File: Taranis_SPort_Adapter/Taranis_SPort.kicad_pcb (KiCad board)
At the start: 2 copper layers, 22.9 x 17.8 mm, 12 parts, among them J1 CONN_01X04, J2 CONN_01X05, J3 CONN_01X04, Q1 DMG6602SVT, U1 MCP1754ST-3302E/MB-fixed

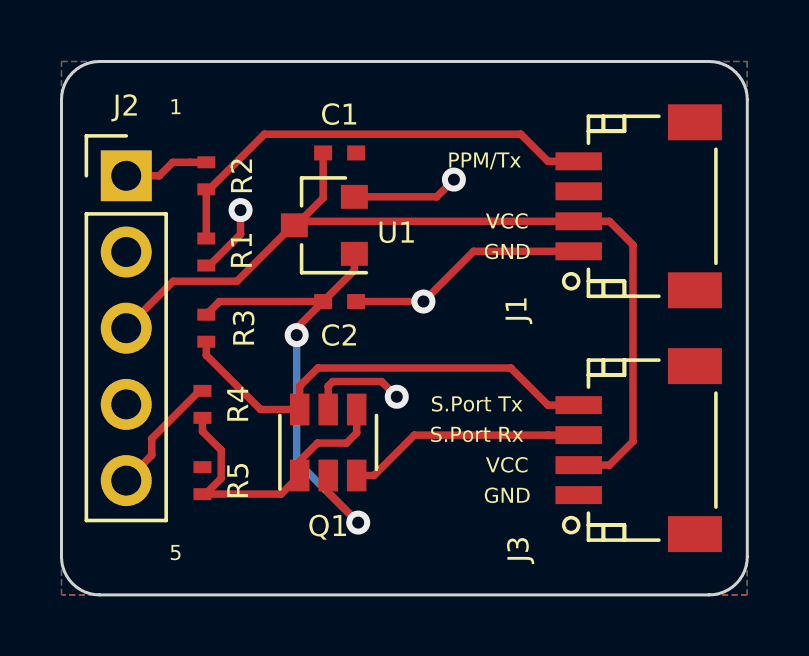
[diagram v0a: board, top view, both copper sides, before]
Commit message: Adds a Dual Interter board and Fixes the voltage regulator pin ordering on the SPort adapter board.
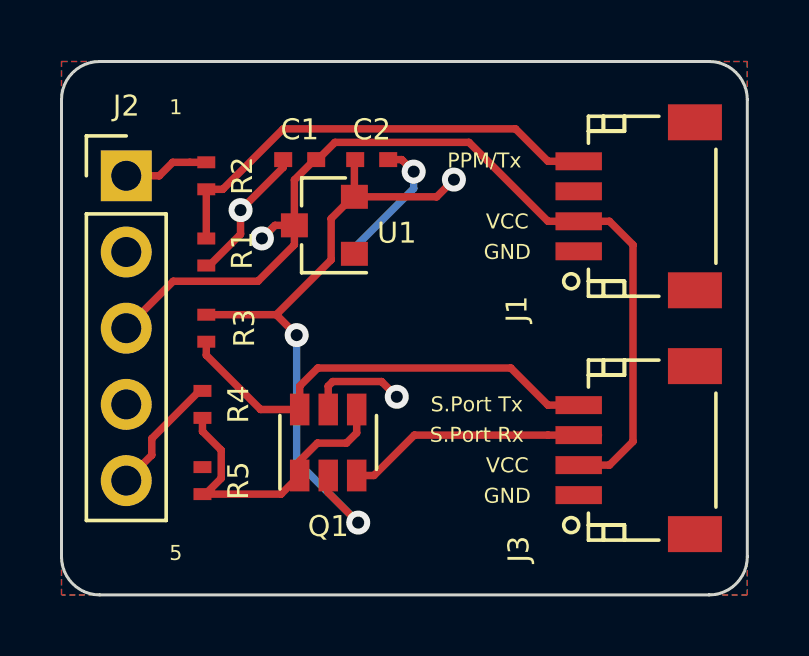
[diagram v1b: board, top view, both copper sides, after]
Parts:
- U1: value MCP1754ST-3302E/MB-fixed -> MCP1754ST-3302E/MB-SOT-23
- moved C2 4.85 mm to (160.2, 103.6)
- moved C1 1.35 mm to (157.8, 103.6), turned to 180 degrees
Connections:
- J1 pad 3: Net-(J1-Pad3) -> (no net)
- J2 pad 2: Net-(J2-Pad2) -> (no net)
- U1 pad 1: +3V3 -> GND
- U1 pad 2: GND -> +3V3
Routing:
- net +3V3: track 16.8 -> 22.5 mm, vias 2 -> 3
- net GND: track 17.4 -> 12.5 mm, vias 4 -> 3
- net VCC: track 30.4 -> 33.1 mm, vias 0 -> 1
- net Net-(J1-Pad3): track 0.66 -> 0.00 mm

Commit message: Fixed some unconnected grounds in SPort apdater.
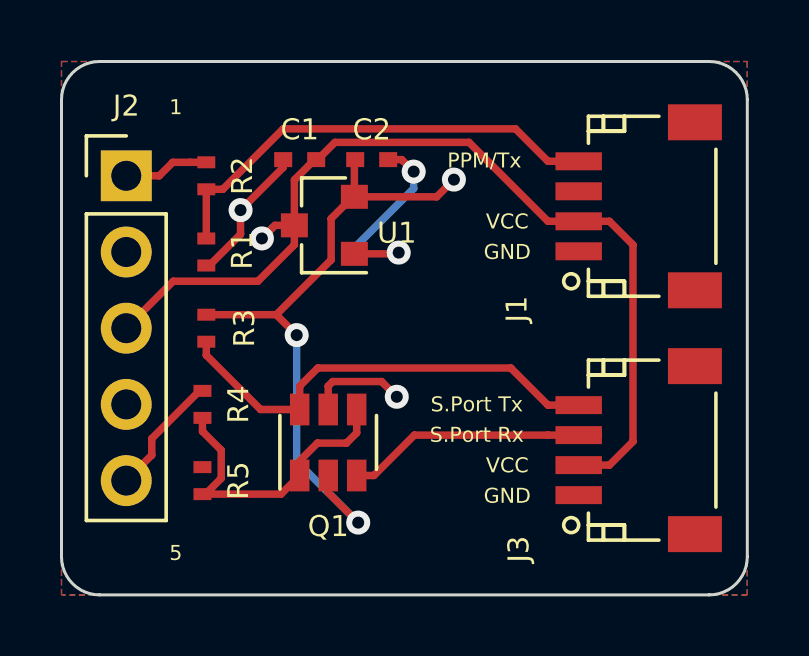
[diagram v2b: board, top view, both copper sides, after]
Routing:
- net GND: track 12.5 -> 14.0 mm, vias 3 -> 4
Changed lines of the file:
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@@
   (general
     (links 25)
-    (no_connects 1)
+    (no_connects 0)
     (area 149.809999 100.279999 172.770001 118.160001)
     (thickness 1.6)
     (drawings 19)
-    (tracks 101)
+    (tracks 104)
     (zones 0)
     (modules 12)
@@
   (segment (start 168.1245 113.784) (end 168.91 112.9985) (width 0.25) (layer F.Cu) (net 1))
   (segment (start 152.019 109.22) (end 152.146 109.22) (width 0.25) (layer F.Cu) (net 1))
+  (segment (start 159.623 106.741) (end 161.059 106.741) (width 0.25) (layer F.Cu) (net 2))
+  (segment (start 161.059 106.741) (end 161.1 106.7) (width 0.25) (layer F.Cu) (net 2))
+  (via (at 161.1 106.7) (size 0.8) (drill 0.4) (layers F.Cu B.Cu) (net 2))
   (segment (start 161.6 104) (end 161.6 104.565685) (width 0.25) (layer B.Cu) (net 2))
   (segment (start 161.6 104.565685) (end 159.6 106.565685) (width 0.25) (layer B.Cu) (net 2))

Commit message: Adds S.Port Rx to second (PPM) connector on S.Port Adapter.
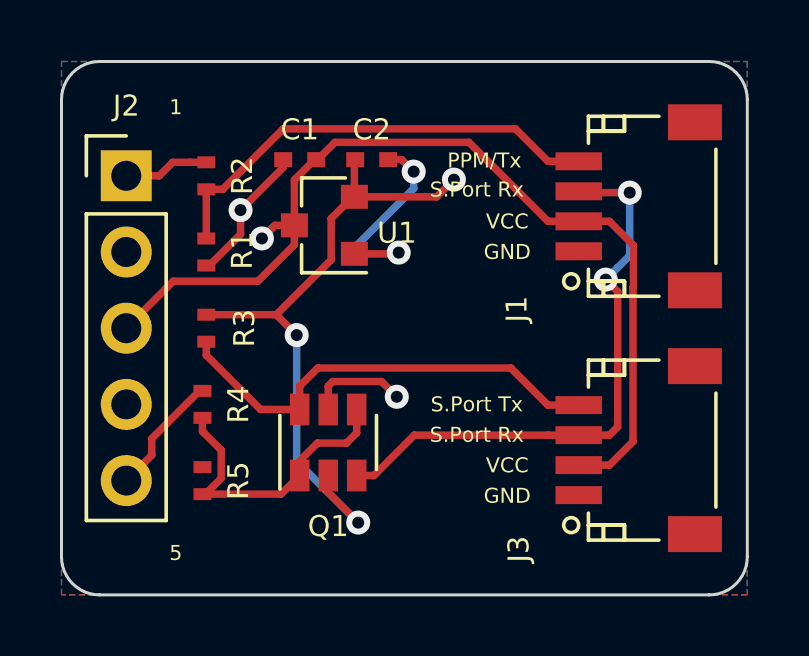
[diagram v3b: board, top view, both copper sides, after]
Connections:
- J1 pad 3: (no net) -> Net-(J1-Pad3)
- J3 pad 3: Net-(J3-Pad3) -> Net-(J1-Pad3)
- Q1 pad 3: Net-(J3-Pad3) -> Net-(J1-Pad3)
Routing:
- net Net-(J1-Pad3): track 0.00 -> 20.1 mm, vias 0 -> 2
- net Net-(J3-Pad3): track 8.62 -> 0.00 mm
